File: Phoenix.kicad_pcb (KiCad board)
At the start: 2 copper layers, 86.4 x 40.6 mm, 102 parts, among them J1 Conn_01x02_Male, J2 Mini USB Female, J3 Battery Connector, J4 Pyro Connectors, Q1 2N7000, Q2 BSS84, Q3 IRFML8244TRPBF, Q4 IRFML8244TRPBF, Q5 IRFML8244TRPBF, Q6 IRFML8244TRPBF, U1 RP2040, U3 AMS1117-3.3, U4 I3G4250D, U5 MS5637-02BA03, U6 ADXL343, U8 Si4468/7, U9 L70B-M39, Y1 12MHz, Y2 26MHz

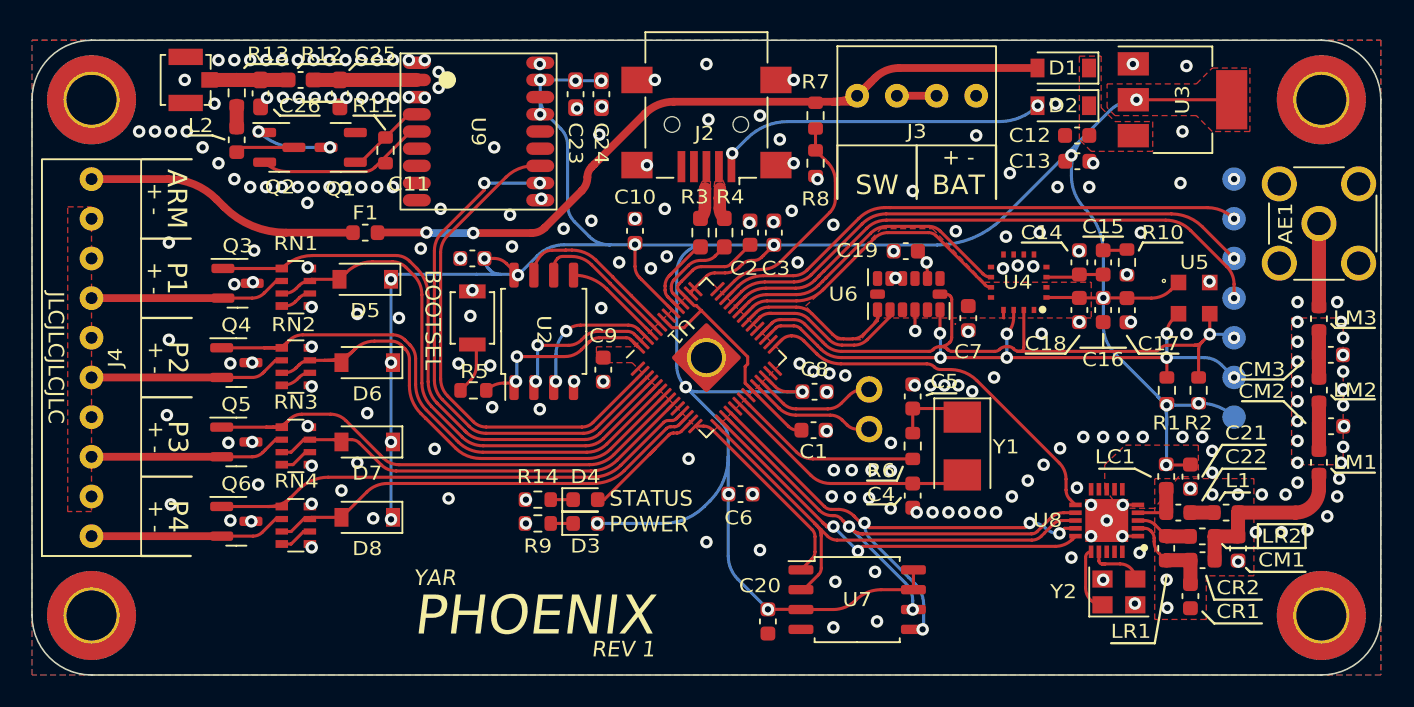
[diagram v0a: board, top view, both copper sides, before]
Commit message: rev2 changes excluding pyro
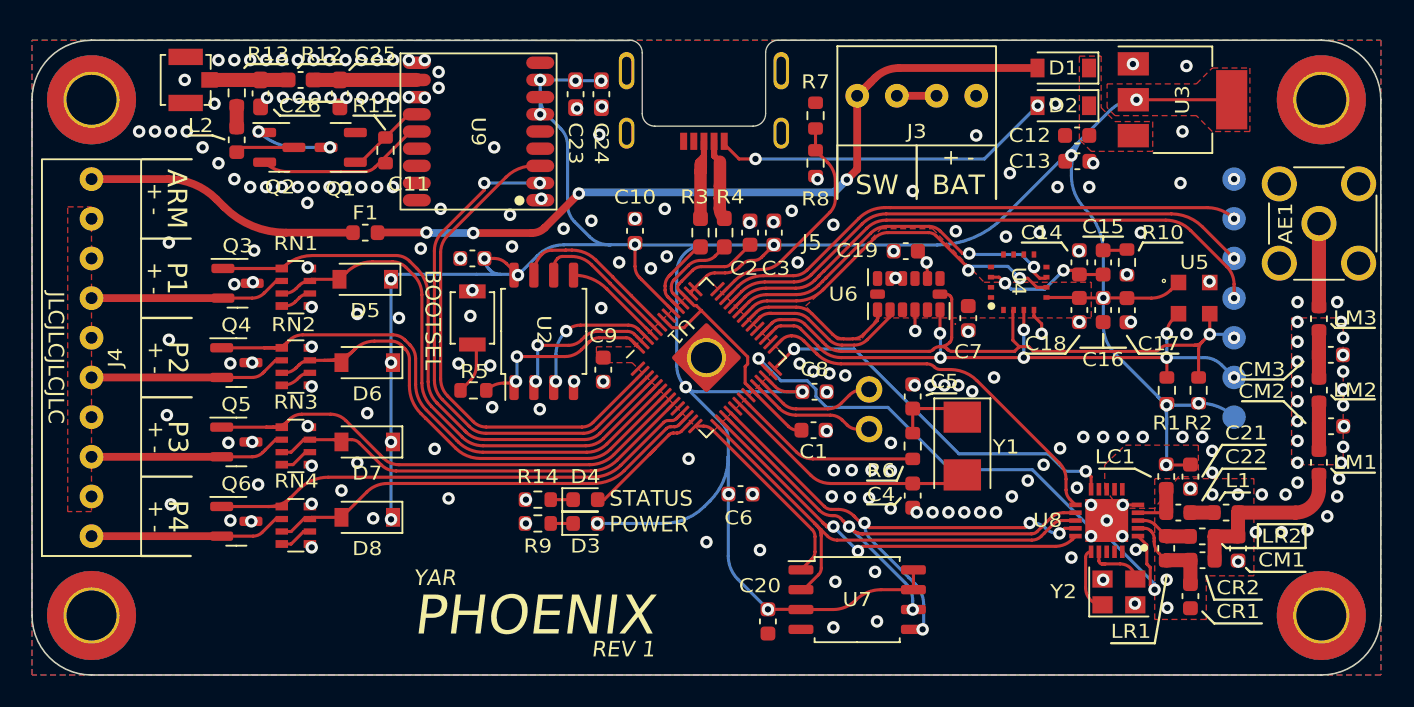
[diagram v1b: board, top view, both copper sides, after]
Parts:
- removed J2: Mini USB Female, Connector_USB:USB_Mini-B_Lumberg_2486_01_Horizontal
- added J5: USB_B_Micro, YAR_Connectors:USB-micro-b-molex-0476420001, F.Cu at (102.7, 27.8)
- turned U4 to 180 degrees
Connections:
- U1 pad 27: unconnected-(U1-Pad27) -> RADIO-SDN
- U1 pad 28: unconnected-(U1-Pad28) -> RADIO_GPIO1
- U8 pad 1: GND -> RADIO-SDN
- U8 pad 10: unconnected-(U8-Pad10) -> RADIO_GPIO1
- U9 pad 9: GND -> unconnected-(U9-~{Reset}-Pad9)
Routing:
- net RADIO-SDN: track 0.00 -> 37.1 mm, vias 0 -> 2
- net RADIO_GPIO1: track 0.00 -> 25.0 mm, vias 0 -> 2
- net Net-(U4-PLLFILT): track 3.70 -> 8.35 mm, vias 0 -> 2
- net /Power Supply/D+: track 1.98 -> 6.30 mm
- net /Accelerometer/Gyro2: track 19.2 -> 23.1 mm, vias 0 -> 2
- net /Accelerometer/Gyro1: track 19.4 -> 23.3 mm, vias 0 -> 2
- net /Power Supply/D-: track 1.99 -> 5.17 mm
- net +BATT: track 49.6 -> 49.9 mm, vias 2 -> 4
- net GND: track 12.0 -> 12.2 mm, vias 241 -> 229
- removed copper zone on F.Cu, net /Power Supply/D+
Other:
- outline, holes or cut-outs redrawn

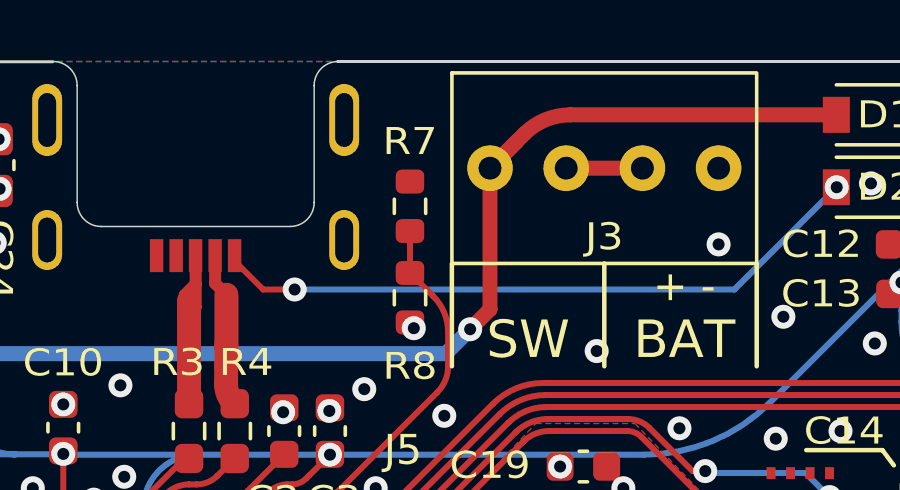
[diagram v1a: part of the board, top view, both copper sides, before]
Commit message: Fixed unrouted battery track
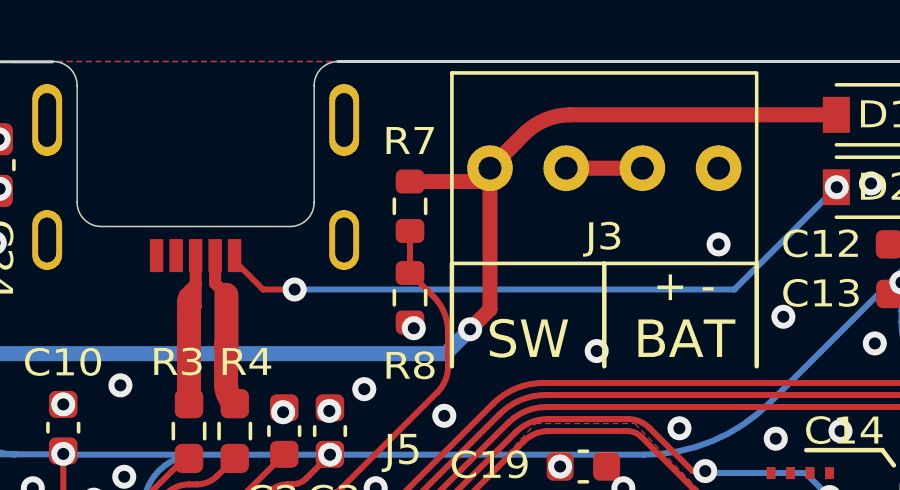
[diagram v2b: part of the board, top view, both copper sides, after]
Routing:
- net +BATT: track 49.9 -> 52.8 mm
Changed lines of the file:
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@@
   (segment (start 87.940177 38.155107) (end 91.69422 38.155107) (width 0.5) (layer "F.Cu") (net 9))
   (segment (start 112.522 29.3685) (end 113.411 28.4795) (width 0.5) (layer "F.Cu") (net 9))
+  (segment (start 112.077 29.8135) (end 112.522 29.3685) (width 0.5) (layer "F.Cu") (net 9))
+  (segment (start 109.855 29.8135) (end 112.077 29.8135) (width 0.5) (layer "F.Cu") (net 9))
   (segment (start 112.522 34.0755) (end 111.86 34.7375) (width 0.5) (layer "F.Cu") (net 9))
   (segment (start 84.943752 38.120205) (end 81.824795 38.120205) (width 0.5) (layer "F.Cu") (net 9))
@@
     (connect_pads yes (clearance 0.2))
     (min_thickness 0.2) (filled_areas_thickness no)
-    (fill (thermal_gap 0.508) (thermal_bridge_width 0.508))
+    (fill yes (thermal_gap 0.508) (thermal_bridge_width 0.508))
     (polygon
       (pts
@@
     (connect_pads yes (clearance 0.15))
     (min_thickness 0.15) (filled_areas_thickness no)
-    (fill (thermal_gap 0.2) (thermal_bridge_width 0.5))
+    (fill yes (thermal_gap 0.2) (thermal_bridge_width 0.5))
     (polygon
       (pts
@@
     (connect_pads yes (clearance 0.2))
     (min_thickness 0.2) (filled_areas_thickness no)
-    (fill (thermal_gap 0.508) (thermal_bridge_width 0.508))
+    (fill yes (thermal_gap 0.508) (thermal_bridge_width 0.508))
     (polygon
       (pts
@@
     (connect_pads thru_hole_only (clearance 0.5))
     (min_thickness 0.254) (filled_areas_thickness no)
-    (fill (thermal_gap 0.508) (thermal_bridge_width 0.508))
+    (fill yes (thermal_gap 0.508) (thermal_bridge_width 0.508))
     (polygon
       (pts
@@
     (connect_pads yes (clearance 0.2))
     (min_thickness 0.2) (filled_areas_thickness no)
-    (fill (thermal_gap 0.508) (thermal_bridge_width 0.508))
+    (fill yes (thermal_gap 0.508) (thermal_bridge_width 0.508))
     (polygon
       (pts
@@
     (connect_pads yes (clearance 0.2))
     (min_thickness 0.2) (filled_areas_thickness no)
-    (fill (thermal_gap 0.508) (thermal_bridge_width 0.508))
+    (fill yes (thermal_gap 0.508) (thermal_bridge_width 0.508))
     (polygon
       (pts
@@
     (connect_pads thru_hole_only (clearance 0.5))
     (min_thickness 0.254) (filled_areas_thickness no)
-    (fill (thermal_gap 0.508) (thermal_bridge_width 0.508))
+    (fill yes (thermal_gap 0.508) (thermal_bridge_width 0.508))
     (polygon
       (pts
@@
     (connect_pads thru_hole_only (clearance 0.2))
     (min_thickness 0.2) (filled_areas_thickness no)
-    (fill (thermal_gap 0.508) (thermal_bridge_width 0.508))
+    (fill yes (thermal_gap 0.508) (thermal_bridge_width 0.508))
     (polygon
       (pts
@@
     (connect_pads yes (clearance 0.2))
     (min_thickness 0.2) (filled_areas_thickness no)
-    (fill (thermal_gap 0.508) (thermal_bridge_width 0.508))
+    (fill yes (thermal_gap 0.508) (thermal_bridge_width 0.508))
     (polygon
       (pts
@@
     (connect_pads thru_hole_only (clearance 0.5))
     (min_thickness 0.254) (filled_areas_thickness no)
-    (fill (thermal_gap 0.508) (thermal_bridge_width 0.508))
+    (fill yes (thermal_gap 0.508) (thermal_bridge_width 0.508))
     (polygon
       (pts
@@
     (connect_pads (clearance 0.2))
     (min_thickness 0.2) (filled_areas_thickness no)
-    (fill (thermal_gap 0.2) (thermal_bridge_width 0.2))
-    (polygon
-      (pts
+    (fill yes (thermal_gap 0.2) (thermal_bridge_width 0.2))
+    (polygon
+      (pts

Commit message: Rev 1B
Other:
- board text added: "Phoenix Rev 1 AG, CH 2023"
- board text added: "REV 1B"
- board text removed: "Phoenix Rev 1 AG & WH 2022"
- board text removed: "REV 1"
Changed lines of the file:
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@@
     (effects (font (size 1 1) (thickness 0.15)) (justify mirror))
   )
-  (gr_text "Phoenix Rev 1\nAG & WH 2022" (at 66.548 46.1325 270) (layer "B.SilkS")
+  (gr_text "Phoenix Rev 1\nAG, CH 2023" (at 66.548 46.1325 270) (layer "B.SilkS")
     (effects (font (size 1 1) (thickness 0.15)) (justify mirror))
   )
@@
     (effects (font (size 1 1) (thickness 0.15)) (justify left))
   )
-  (gr_text "REV 1" (at 97.536 64.8015) (layer "F.SilkS")
+  (gr_text "REV 1B" (at 97.536 64.8015) (layer "F.SilkS")
     (effects (font (size 1 1) (thickness 0.15) italic))
   )
